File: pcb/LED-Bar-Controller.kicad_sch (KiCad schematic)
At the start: 30 parts, among them J1 Conn_01x03, J2 USB_C, J3 Serial, Q1 AO3400A, Q2 AO3400A, SW1 Power, SW2 Color, SW3 Bright-, SW4 Bright+, U1 ESP32-WROOM-32, U2 AMS1117-3.3

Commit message: feat: add JLC part numbers for all basic parts
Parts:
- C1, C2, C3: LCSC (none) -> C7171
- C4, C6: LCSC (none) -> C1525
- C5: LCSC (none) -> C15525
- D1: LCSC (none) -> C2286
- Q1, Q2: LCSC (none) -> C20917
- R1, R3: LCSC (none) -> C25076
- R10: LCSC (none) -> C25744
- R11: LCSC (none) -> C23228
- R12, R2, R4, R5, R6, R7: LCSC (none) -> C25741
- R8, R9: LCSC (none) -> C25905
- U2: LCSC (none) -> C6186
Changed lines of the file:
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@@
+      (effects (font (size 1.27 1.27)) hide)
+    )
+    (property "LCSC" "" (at 173.99 58.42 0)
       (effects (font (size 1.27 1.27)) hide)
     )
@@
       (effects (font (size 1.27 1.27)) (justify left) hide)
     )
+    (property "LCSC" "C20917" (at 130.81 102.87 0)
+      (effects (font (size 1.27 1.27)) hide)
+    )
     (pin "1")
     (pin "2")
@@
       (effects (font (size 1.27 1.27)) hide)
     )
+    (property "LCSC" "C25741" (at 156.21 45.72 0)
+      (effects (font (size 1.27 1.27)) hide)
+    )
     (pin "1")
     (pin "2")
@@
       (effects (font (size 1.27 1.27)) hide)
     )
+    (property "LCSC" "C25905" (at 82.55 162.56 0)
+      (effects (font (size 1.27 1.27)) hide)
+    )
     (pin "1")
     (pin "2")
@@
       (effects (font (size 1.27 1.27)) hide)
     )
+    (property "LCSC" "C7171" (at 85.09 147.32 0)
+      (effects (font (size 1.27 1.27)) hide)
+    )
     (pin "1")
     (pin "2")
@@
       (effects (font (size 1.27 1.27)) hide)
     )
+    (property "LCSC" "C25741" (at 120.65 45.72 0)
+      (effects (font (size 1.27 1.27)) hide)
+    )
     (pin "1")
     (pin "2")
@@
       (effects (font (size 1.27 1.27)) hide)
     )
+    (property "LCSC" "C1525" (at 52.07 35.56 0)
+      (effects (font (size 1.27 1.27)) hide)
+    )
     (pin "1")
     (pin "2")
@@
     )
     (property "Datasheet" "~" (at 138.43 45.72 0)
+      (effects (font (size 1.27 1.27)) hide)
+    )
+    (property "LCSC" "C25741" (at 138.43 45.72 0)
       (effects (font (size 1.27 1.27)) hide)
     )
@@
       (effects (font (size 1.27 1.27)) (justify left) hide)
     )
+    (property "LCSC" "C20917" (at 171.45 102.87 0)
+      (effects (font (size 1.27 1.27)) hide)
+    )
     (pin "1")
     (pin "2")
@@
       (effects (font (size 1.27 1.27)) hide)
     )
+    (property "LCSC" "C25744" (at 30.48 36.83 0)
+      (effects (font (size 1.27 1.27)) hide)
+    )
     (pin "1")
     (pin "2")
@@
     )
     (property "Datasheet" "~" (at 52.07 27.94 0)
+      (effects (font (size 1.27 1.27)) hide)
+    )
+    (property "LCSC" "C15525" (at 52.07 27.94 0)
       (effects (font (size 1.27 1.27)) hide)
     )
@@
       (effects (font (size 1.27 1.27)) hide)
     )
+    (property "LCSC" "" (at 120.65 58.42 0)
+      (effects (font (size 1.27 1.27)) hide)
+    )
     (pin "1")
     (pin "2")
@@
       (effects (font (size 1.27 1.27)) hide)
     )
+    (property "LCSC" "C2286" (at 185.42 58.42 0)
+      (effects (font (size 1.27 1.27)) hide)
+    )
     (pin "1")
     (pin "2")
@@
       (effects (font (size 1.27 1.27)) hide)
     )
+    (property "LCSC" "C25741" (at 173.99 45.72 0)
+      (effects (font (size 1.27 1.27)) hide)
+    )
     (pin "1")
     (pin "2")
@@
     )
     (property "Datasheet" "~" (at 93.98 48.26 0)
+      (effects (font (size 1.27 1.27)) hide)
+    )
+    (property "LCSC" "" (at 93.98 48.26 0)
       (effects (font (size 1.27 1.27)) hide)
     )
@@
       (effects (font (size 1.27 1.27)) hide)
     )
+    (property "LCSC" "C25076" (at 161.29 102.87 0)
+      (effects (font (size 1.27 1.27)) hide)
+    )
     (pin "1")
     (pin "2")
@@
     )
     (property "Datasheet" "https://www.espressif.com/sites/default/files/documentation/esp32-wroom-32_datasheet_en.pdf" (at 49.53 72.39 0)
+      (effects (font (size 1.27 1.27)) hide)
+    )
+    (property "LCSC" "" (at 57.15 73.66 0)
       (effects (font (size 1.27 1.27)) hide)
     )
@@
       (effects (font (size 1.27 1.27)) hide)
     )
+    (property "LCSC" "C25741" (at 115.57 107.95 0)
+      (effects (font (size 1.27 1.27)) hide)
+    )
     (pin "1")
     (pin "2")
@@
     )
     (property "Datasheet" "~" (at 113.03 147.32 0)
+      (effects (font (size 1.27 1.27)) hide)
+    )
+    (property "LCSC" "C7171" (at 113.03 147.32 0)
       (effects (font (size 1.27 1.27)) hide)
     )
@@
       (effects (font (size 1.27 1.27)) hide)
     )
+    (property "LCSC" "" (at 138.43 58.42 0)
+      (effects (font (size 1.27 1.27)) hide)
+    )
     (pin "1")
     (pin "2")
@@
     )
     (property "Datasheet" "~" (at 30.48 48.26 0)
+      (effects (font (size 1.27 1.27)) hide)
+    )
+    (property "LCSC" "C1525" (at 30.48 48.26 0)
       (effects (font (size 1.27 1.27)) hide)
     )
@@
       (effects (font (size 1.27 1.27)) hide)
     )
+    (property "LCSC" "" (at 156.21 58.42 0)
+      (effects (font (size 1.27 1.27)) hide)
+    )
     (pin "1")
     (pin "2")
@@
       (effects (font (size 1.27 1.27)) hide)
     )
+    (property "LCSC" "C6186" (at 95.25 142.24 0)
+      (effects (font (size 1.27 1.27)) hide)
+    )
     (pin "1")
     (pin "2")
@@
       (effects (font (size 1.27 1.27)) hide)
     )
+    (property "LCSC" "C23228" (at 185.42 45.72 0)
+      (effects (font (size 1.27 1.27)) hide)
+    )
     (pin "1")
     (pin "2")
@@
       (effects (font (size 1.27 1.27)) hide)
     )
+    (property "LCSC" "" (at 181.61 92.71 0)
+      (effects (font (size 1.27 1.27)) hide)
+    )
     (pin "1")
     (pin "2")
@@
       (effects (font (size 1.27 1.27)) hide)
     )
+    (property "LCSC" "C25905" (at 76.2 162.56 0)
+      (effects (font (size 1.27 1.27)) hide)
+    )
     (pin "1")
     (pin "2")
@@
       (effects (font (size 1.27 1.27)) hide)
     )
+    (property "LCSC" "C25741" (at 156.21 107.95 0)
+      (effects (font (size 1.27 1.27)) hide)
+    )
     (pin "1")
     (pin "2")
@@
       (effects (font (size 1.27 1.27)) hide)
     )
+    (property "LCSC" "C25076" (at 120.65 102.87 0)
+      (effects (font (size 1.27 1.27)) hide)
+    )
     (pin "1")
     (pin "2")
@@
     )
     (property "Datasheet" "https://www.usb.org/sites/default/files/documents/usb_type-c.zip" (at 57.15 149.86 0)
+      (effects (font (size 1.27 1.27)) hide)
+    )
+    (property "LCSC" "" (at 57.15 149.86 0)
       (effects (font (size 1.27 1.27)) hide)
     )
@@
       (effects (font (size 1.27 1.27)) hide)
     )
+    (property "LCSC" "C7171" (at 105.41 147.32 0)
+      (effects (font (size 1.27 1.27)) hide)
+    )

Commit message: fix: switch WW and CW positions
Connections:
- net CW: now also J1.3 (Pin_3), Q2.3 (D); no longer J1.2 (Pin_2), Q1.3 (D)
- net Gcw: now also Q2.1 (G), R3.2; no longer Q1.1 (G), R1.2
- net Gww: now also Q1.1 (G), R1.2; no longer Q2.1 (G), R3.2
- net PWM_CW: now also R3.1, R4.1, U1.30 (IO18); no longer R1.1, R2.1, U1.31 (IO19)
- net PWM_WW: now also R1.1, R2.1, U1.31 (IO19); no longer R3.1, R4.1, U1.30 (IO18)
- net WW: now also J1.2 (Pin_2), Q1.3 (D); no longer J1.3 (Pin_3), Q2.3 (D)
- no-connect marks 12 -> 23
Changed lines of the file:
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@@
   (junction (at 138.43 50.8) (diameter 0) (color 0 0 0 0)
   )
+  (no_connect (at 72.39 96.52))
+  (no_connect (at 72.39 99.06))
+  (no_connect (at 72.39 93.98))
+  (no_connect (at 72.39 63.5))
+  (no_connect (at 72.39 101.6))
   (no_connect (at 72.39 66.04))
+  (no_connect (at 72.39 71.12))
   (no_connect (at 41.91 83.82))
   (no_connect (at 41.91 78.74))
+  (no_connect (at 72.39 68.58))
   (no_connect (at 72.39 55.88))
+  (no_connect (at 72.39 86.36))
   (no_connect (at 41.91 50.8))
   (no_connect (at 72.39 53.34))
+  (no_connect (at 72.39 60.96))
   (no_connect (at 41.91 86.36))
+  (no_connect (at 72.39 91.44))
   (no_connect (at 41.91 48.26))
   (no_connect (at 72.39 58.42))
   (no_connect (at 41.91 76.2))
   (no_connect (at 41.91 73.66))
+  (no_connect (at 72.39 88.9))
   (no_connect (at 41.91 81.28))
   (wire (pts (xy 156.21 50.8) (xy 156.21 53.34))
@@
     (effects (font (size 1.27 1.27)) (justify left bottom))
   )
-  (label "PWM_WW" (at 72.39 73.66 0) (fields_autoplaced)
+  (label "PWM_WW" (at 72.39 76.2 0) (fields_autoplaced)
     (effects (font (size 1.27 1.27)) (justify left bottom))
   )
@@
     (effects (font (size 1.27 1.27)) (justify left bottom))
   )
-  (label "Gww" (at 163.83 102.87 0) (fields_autoplaced)
+  (label "Gww" (at 123.19 102.87 0) (fields_autoplaced)
     (effects (font (size 1.27 1.27)) (justify left bottom))
   )
@@
     (effects (font (size 1.27 1.27)) (justify left bottom))
   )
-  (label "WW" (at 176.53 95.25 180) (fields_autoplaced)
+  (label "WW" (at 176.53 92.71 180) (fields_autoplaced)
     (effects (font (size 1.27 1.27)) (justify right bottom))
   )
@@
     (effects (font (size 1.27 1.27)) (justify left bottom))
   )
-  (label "PWM_CW" (at 113.03 102.87 180) (fields_autoplaced)
+  (label "PWM_CW" (at 153.67 102.87 180) (fields_autoplaced)
     (effects (font (size 1.27 1.27)) (justify right bottom))
   )
@@
     (effects (font (size 1.27 1.27)) (justify right bottom))
   )
-  (label "CW" (at 176.53 92.71 180) (fields_autoplaced)
-    (effects (font (size 1.27 1.27)) (justify right bottom))
-  )
-  (label "PWM_WW" (at 153.67 102.87 180) (fields_autoplaced)
+  (label "CW" (at 176.53 95.25 180) (fields_autoplaced)
+    (effects (font (size 1.27 1.27)) (justify right bottom))
+  )
+  (label "PWM_WW" (at 113.03 102.87 180) (fields_autoplaced)
     (effects (font (size 1.27 1.27)) (justify right bottom))
   )
@@
     (effects (font (size 1.27 1.27)) (justify left bottom))
   )
-  (label "Gcw" (at 123.19 102.87 0) (fields_autoplaced)
-    (effects (font (size 1.27 1.27)) (justify left bottom))
-  )
-  (label "PWM_CW" (at 72.39 76.2 0) (fields_autoplaced)
-    (effects (font (size 1.27 1.27)) (justify left bottom))
-  )
+  (label "Gcw" (at 163.83 102.87 0) (fields_autoplaced)
+    (effects (font (size 1.27 1.27)) (justify left bottom))
+  )
+  (label "PWM_CW" (at 72.39 73.66 0) (fields_autoplaced)
+    (effects (font (size 1.27 1.27)) (justify left bottom))
+  )

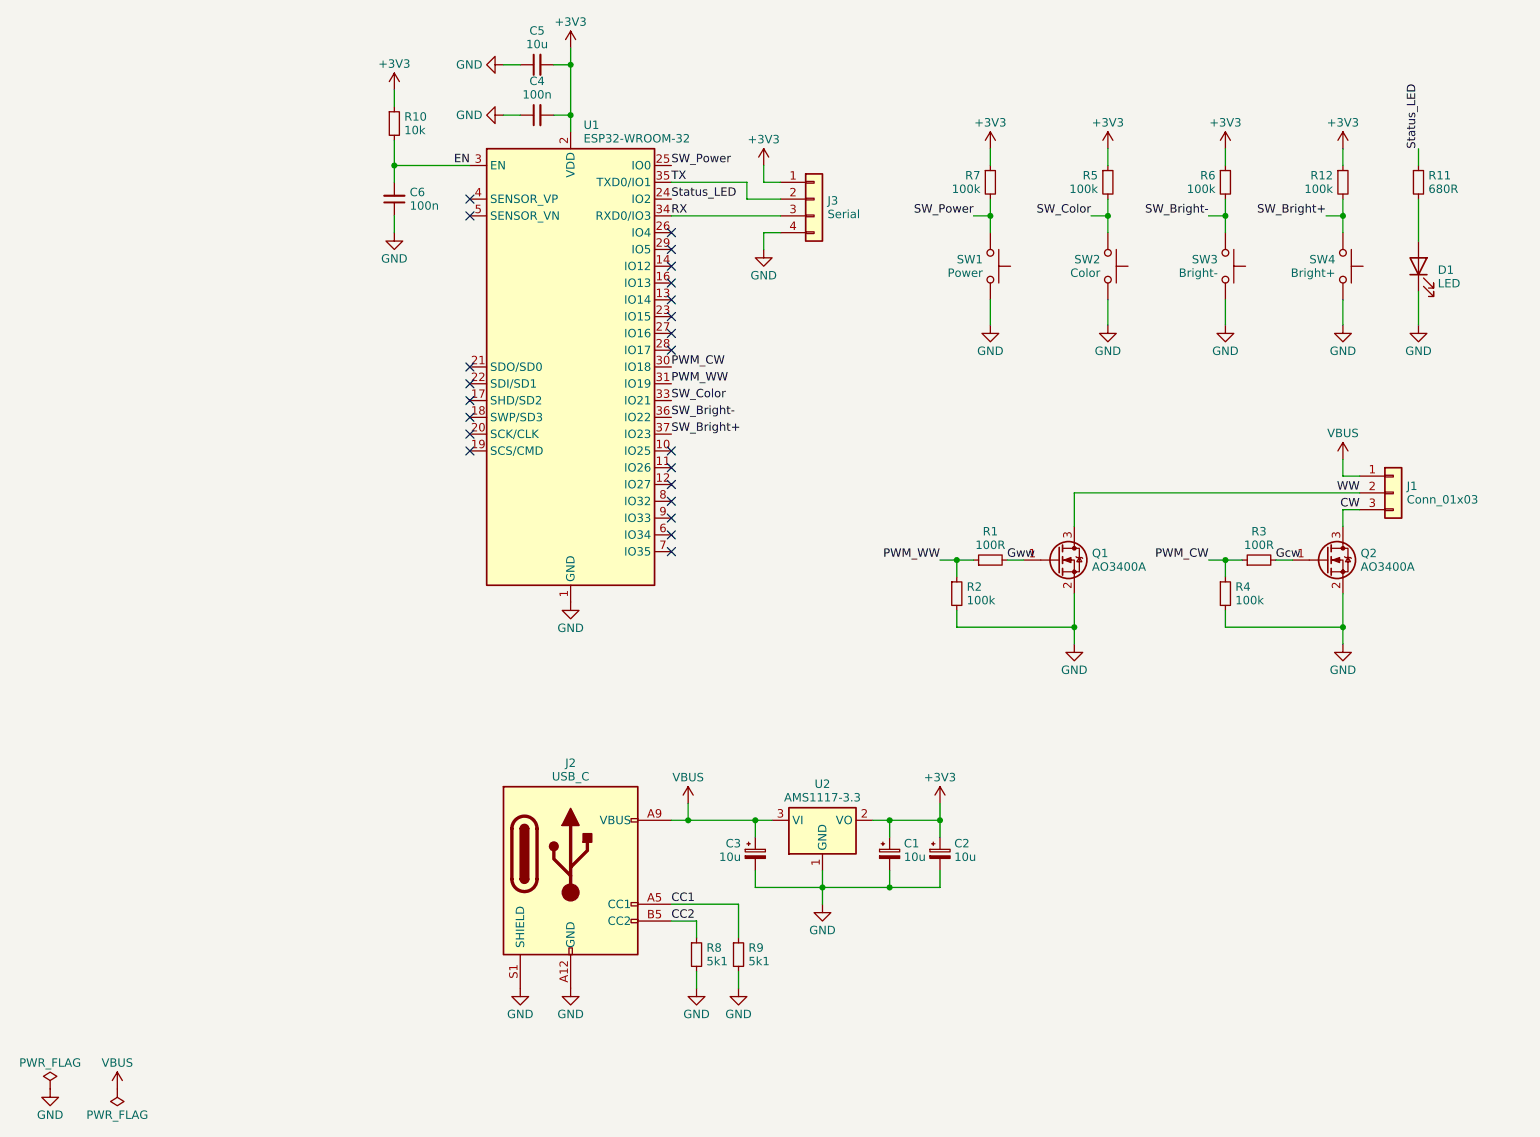
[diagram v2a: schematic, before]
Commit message: feat: change button type
change buttons to type in JLCPCB basic library and change their positions
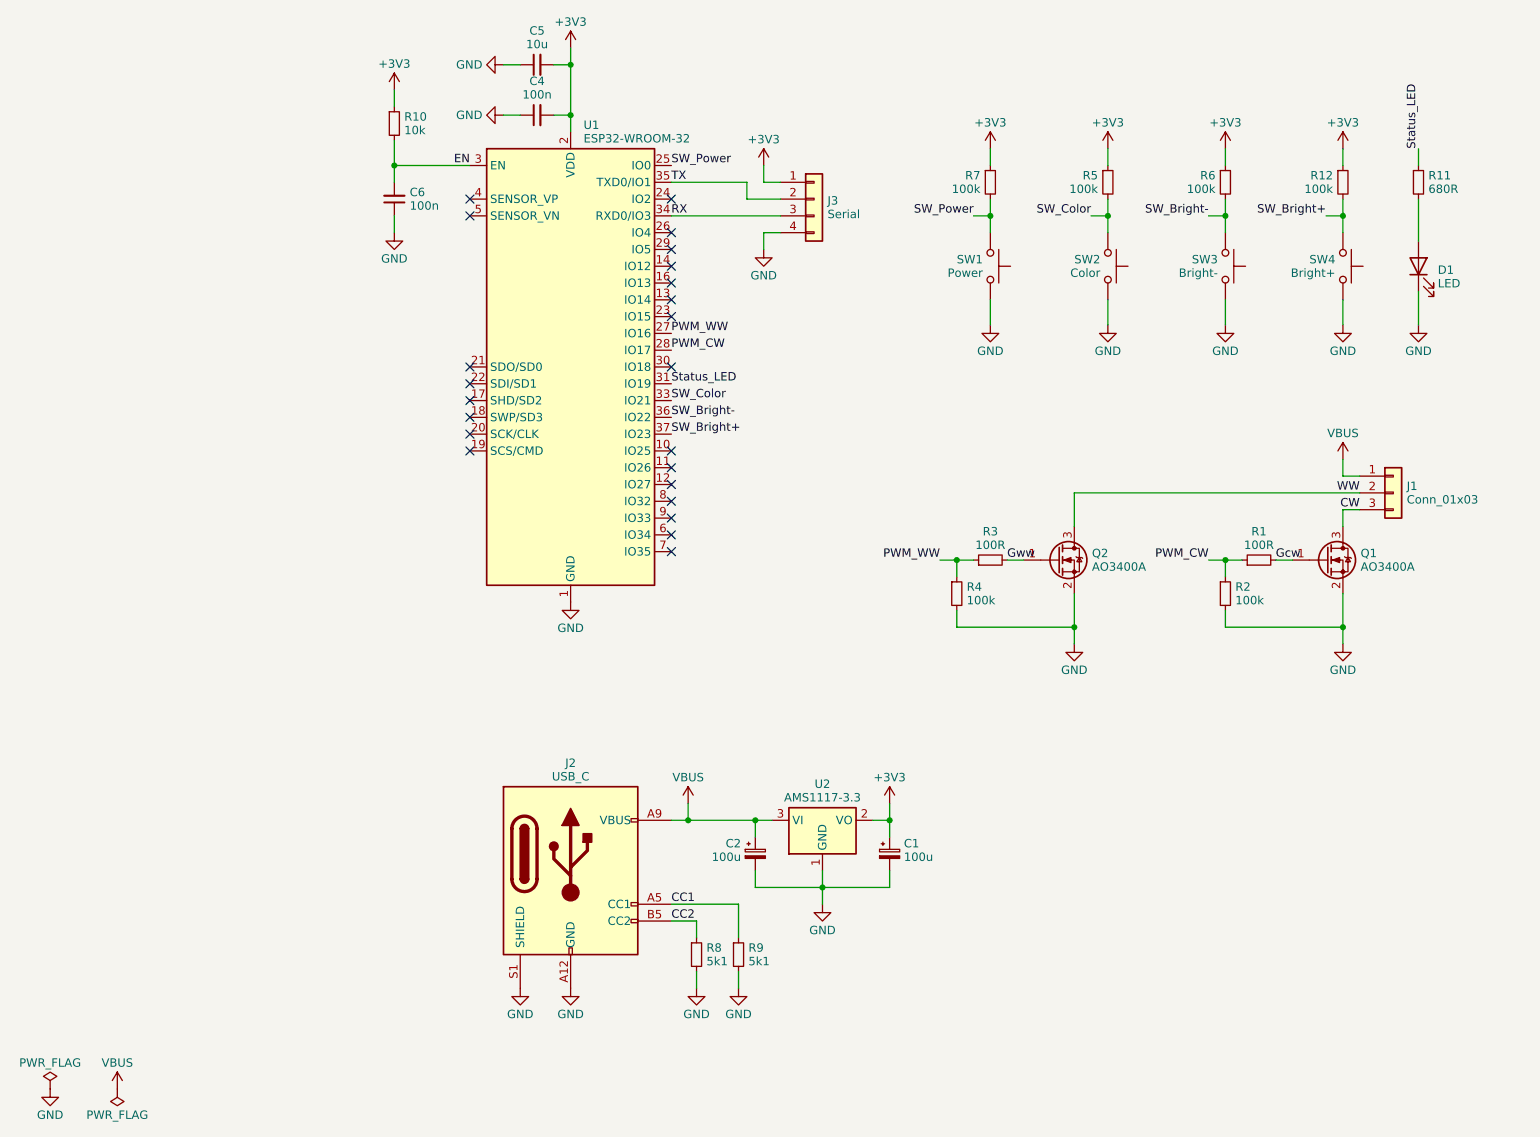
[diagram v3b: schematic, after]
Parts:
- removed C2: 10u, Capacitor_Tantalum_SMD:CP_EIA-3216-18_Kemet-A, symbol Device:C_Polarized_Small
- C1: value 10u -> 100u; footprint Capacitor_Tantalum_SMD:CP_EIA-3216-18_Kemet-A -> Capacitor_Tantalum_SMD:CP_EIA-3528-21_Kemet-B; LCSC C7171 -> C16133
- C2: renamed from C3; value 10u -> 100u; footprint Capacitor_Tantalum_SMD:CP_EIA-3216-18_Kemet-A -> Capacitor_Tantalum_SMD:CP_EIA-3528-21_Kemet-B; LCSC C7171 -> C16133
- SW1, SW2, SW3, SW4: footprint Button_Switch_SMD:SW_Push_1P1T_NO_6x6mm_H9.5mm -> Button_Switch_SMD:SW_Push_1P1T_XKB_TS-1187A; LCSC (none) -> C318884
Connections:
- net CW: now also Q1.3 (D); no longer Q2.3 (D)
- net Gcw: now also Q1.1 (G), R1.2; no longer Q2.1 (G), R3.2
- net Gww: now also Q2.1 (G), R3.2; no longer Q1.1 (G), R1.2
- net PWM_CW: now also R1.1, R2.1, U1.28 (IO17); no longer R3.1, R4.1, U1.30 (IO18)
- net PWM_WW: now also R3.1, R4.1, U1.27 (IO16); no longer R1.1, R2.1, U1.31 (IO19)
- net Status_LED: now also U1.31 (IO19); no longer U1.24 (IO2)
- net WW: now also Q2.3 (D); no longer Q1.3 (D)
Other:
- moved on the sheet: Q1, Q2, R1, R2, R3, R4

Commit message: style: silkscreen cleanup
Renumber parts and clean up silkscreen positioning
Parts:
- renumbered C6 to C1, C5 to C2, C4 to C3, C2 to C4, C1 to C5, J2 to J1, J3 to J2, J1 to J3, Q2 to Q1, Q1 to Q2, R10 to R1, R3 to R10, R2 to R11, R1 to R12, R8 to R2, R9 to R3, R7 to R4, R12 to R7, R11 to R8, R4 to R9
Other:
- moved on the sheet: J3, Q1, Q2, R10, R11, R12, R9
